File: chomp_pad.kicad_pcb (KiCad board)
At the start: 2 copper layers, 1.3 x 17.2 mm, 94 parts, among them J1 SJ-43514, J2 LED, J3 OLED, SW1 SW_PUSH, SW10 SW_PUSH, SW11 SW_PUSH, SW12 SW_PUSH, SW13 SW_PUSH, SW14 SW_PUSH, SW15 SW_PUSH, SW16 SW_PUSH, SW17 SW_PUSH, SW18 SW_PUSH, SW19 SW_PUSH, SW2 SW_PUSH, SW20 SW_PUSH, SW21 SW_PUSH, SW22 SW_PUSH, SW23 SW_PUSH, SW24 SW_PUSH, SW25 SW_PUSH, SW26 SW_PUSH, SW27 SW_PUSH, SW3 SW_PUSH, SW4 SW_PUSH, SW5 SW_PUSH, SW6 SW_PUSH, SW7 SW_PUSH, SW8 SW_PUSH, SW9 SW_PUSH, U1 kbd:ProMicro

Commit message: sleepy
did a lot, need to fix dependencies on footprints but too lazy to
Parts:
- added D28: D, kbd:D3_TH_SMD, F.Cu at (342.9, 133.3)
- added SW28: Rotary_Encoder_Switch, SofleKeyboard-footprint:RotaryEncoder_Alps_EC11E-Switch_Vertical_H20mm-keebio_modified, F.Cu at (345.0, 122.0)
- SW1, SW10, SW11, SW12, SW13, SW14, SW15, SW16, SW17, SW18, SW19, SW2, SW20, SW21, SW22, SW23, SW24, SW25, SW26, SW3, SW4, SW5, SW6, SW7, SW8, SW9: footprint kbd:MX_ALPS_PG1350_noLed -> Lily58-footprint:MX_Socket_18mm
- SW27: footprint kbd:MX_ALPS_PG1350_noLed_1.75u -> Lily58-footprint:MX_Socket_27mm
- moved D1 185.8 mm to (252.1, 246.9)
- moved D12 185.8 mm to (337.1, 169.4)
- moved D13 185.8 mm to (202.0, 247.8)
- moved D16 185.8 mm to (316.9, 189.5)
- moved D18 185.8 mm to (232.0, 249.6)
- moved D19 185.8 mm to (252.1, 249.6)
- moved D20 185.8 mm to (222.0, 246.9)
- moved D22 185.8 mm to (316.9, 192.1)
- moved D24 185.8 mm to (337.1, 172.1)
- moved D3 185.8 mm to (222.0, 249.6)
- moved D4 185.8 mm to (353.4, 153.8)
- moved D5 185.8 mm to (202.0, 250.4)
- moved D8 185.8 mm to (232.0, 246.9)
- moved D9 185.8 mm to (353.4, 156.5)
- moved J1 185.8 mm to (341.4, 158.7)
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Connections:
- net col0 renamed SW28A
- U1 pad 13: unconnected-(U1-Pad13) -> ENCB
- U1 pad 14: unconnected-(U1-Pad14) -> ENCA

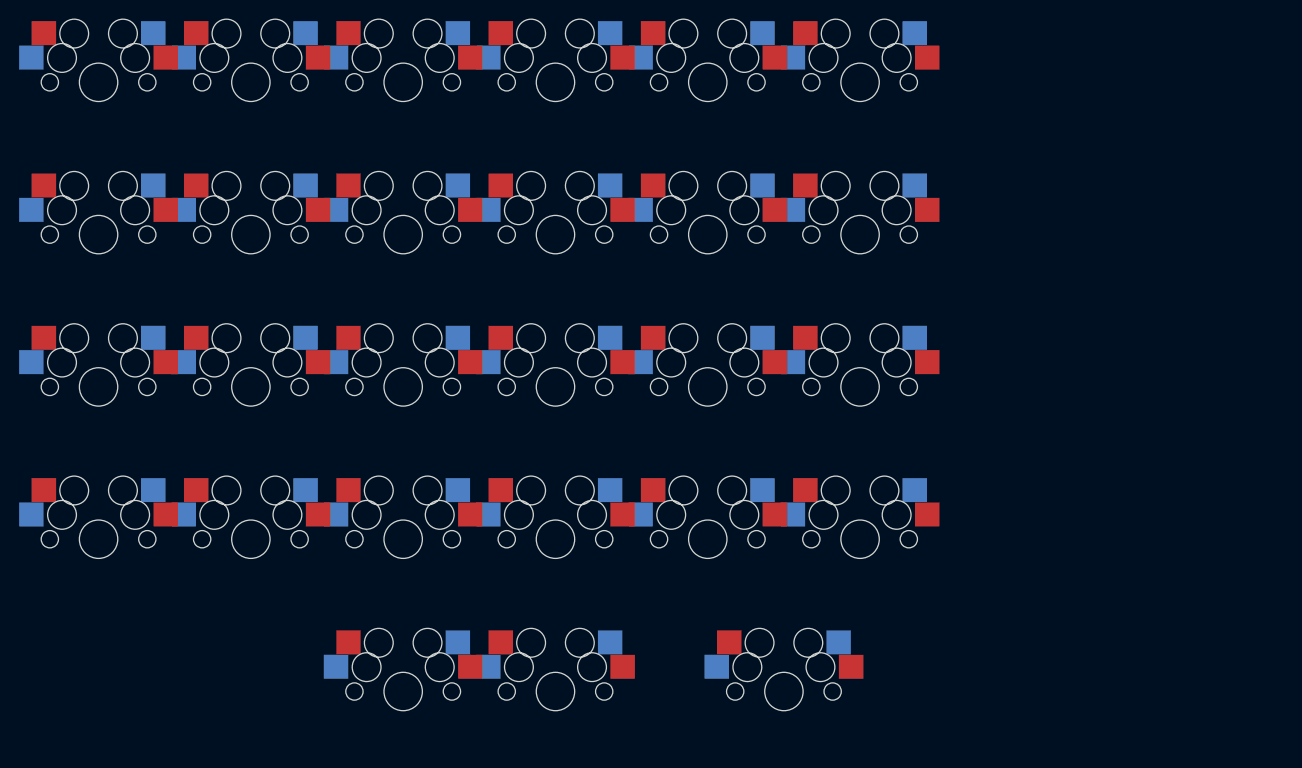
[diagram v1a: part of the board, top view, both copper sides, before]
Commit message: fixed footprint and symbol dependencies
still need to do 3d files but screw that
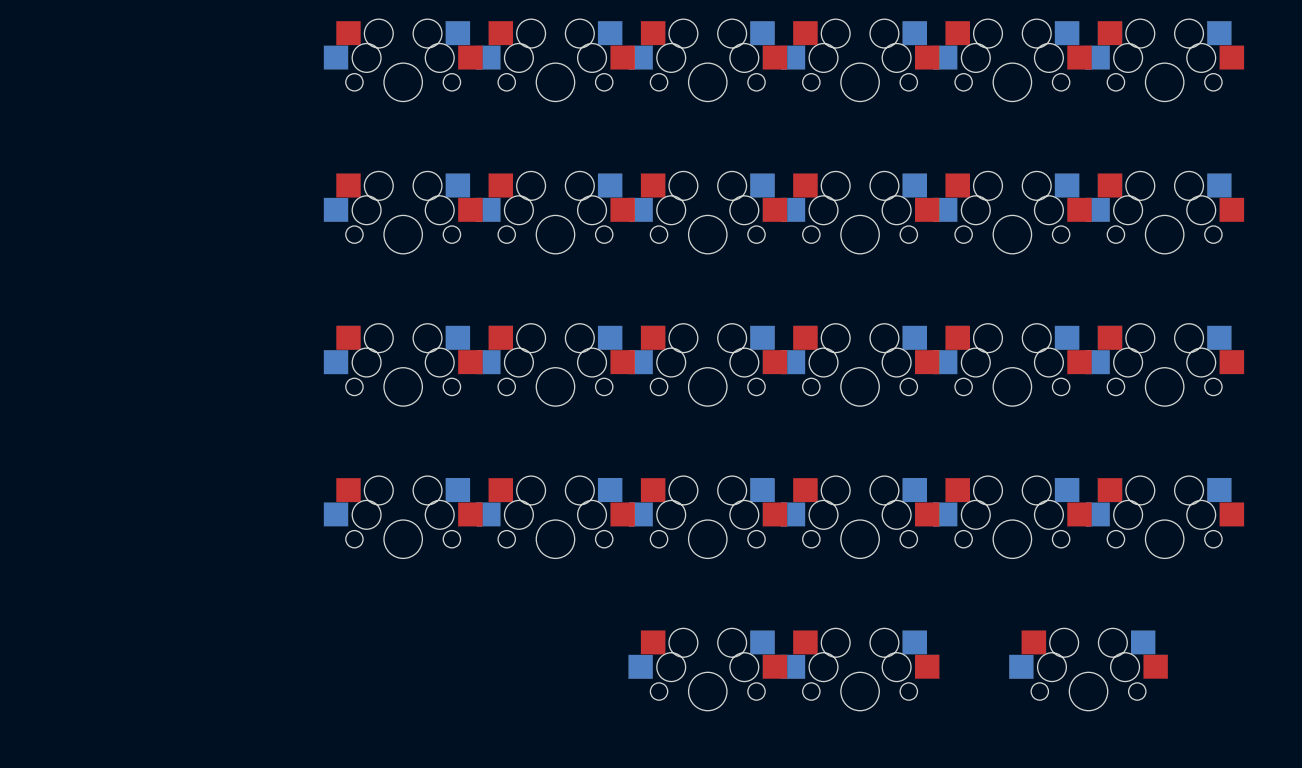
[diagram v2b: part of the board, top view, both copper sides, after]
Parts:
- D1, D10, D11, D12, D13, D14, D15, D16, D17, D18, D19, D2, D20, D21, D22, D23, D24, D25, D26, D27, D28, D3, D4, D5, D6, D7, D8, D9: footprint kbd:D3_TH_SMD -> chomp:D3_TH_SMD
- J1: footprint TRRS:CUI_SJ-43514 -> chomp:CUI_SJ-43514
- J2: footprint kbd:StripLED_rev -> chomp:StripLED_rev
- J3: footprint kbd:OLED -> chomp:OLED
- L1, L2, L3, L4, L5, L6: footprint kbd:SK6812MINI_underglow_rev -> chomp:SK6812MINI_underglow_rev
- L10, L11, L12, L13, L14, L15, L16, L17, L18, L19, L20, L21, L22, L23, L24, L25, L26, L27, L28, L29, L30, L31, L32, L33, L7, L8, L9: footprint kbd:SK6812MINI_rev -> chomp:SK6812MINI_rev
- R1, R2: footprint kbd:R -> chomp:R
- RSW1: footprint kbd:ResetSW -> chomp:ResetSW
- SW1, SW10, SW11, SW12, SW13, SW14, SW15, SW16, SW17, SW18, SW19, SW2, SW20, SW21, SW22, SW23, SW24, SW25, SW26, SW3, SW4, SW5, SW6, SW7, SW8, SW9: footprint Lily58-footprint:MX_Socket_18mm -> chomp:MX_Socket_18mm
- SW27: footprint Lily58-footprint:MX_Socket_27mm -> chomp:MX_Socket_27mm
- SW28: footprint SofleKeyboard-footprint:RotaryEncoder_Alps_EC11E-Switch_Vertical_H20mm-keebio_modified -> chomp:RotaryEncoder_Alps_EC11E-Switch_Vertical_H20mm-keebio_modified
- U1: footprint kbd:ProMicro_v2 -> chomp:ProMicro_v2
- moved SW1 31.8 mm to (63.5, 55.6)
- moved SW10 31.8 mm to (111.1, 71.4)
- moved SW11 31.8 mm to (127.0, 71.4)
- moved SW12 31.8 mm to (142.9, 71.4)
- moved SW13 31.8 mm to (63.5, 87.3)
- moved SW14 31.8 mm to (79.4, 87.3)
- moved SW15 31.8 mm to (95.2, 87.3)
- moved SW16 31.8 mm to (111.1, 87.3)
- moved SW17 31.8 mm to (127.0, 87.3)
- moved SW18 31.8 mm to (142.9, 87.3)
- moved SW19 31.8 mm to (63.5, 103.2)
- moved SW2 31.8 mm to (79.4, 55.6)
- moved SW20 31.8 mm to (79.4, 103.2)
- moved SW21 31.8 mm to (95.2, 103.2)
- moved SW22 31.8 mm to (111.1, 103.2)
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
